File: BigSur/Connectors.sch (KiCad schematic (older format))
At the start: 15 parts, among them J1 XT30, J10 XT30, J11 XT30, J2 XT30, J3 XT30, J4 XT30, J5 XT30, J6 SMD CASTELLATION PKG, J7 XT30, J8 XT30, J9 XT30

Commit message: Added mounting holes, CAN connector,  indicator LEDs, started general purpose relays
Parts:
- removed J6: SMD CASTELLATION PKG, symbol Connector_Generic:Conn_02x21_Counter_Clockwise
- removed J?: XT30, symbol Connector_Generic:Conn_01x02
- added C28, C29: 0.1uF, symbol Device:C
- added D13: NUP2105L, Package_TO_SOT_SMD:SOT-23, symbol Device:D_TVS_x2_AAC
- added H1, H2, H3, H4: Hole, symbol Mechanical:MountingHole_Pad
- added J12: Conn_01x04, symbol Connector_Generic:Conn_01x04
- added J6: XT30, symbol Connector_Generic:Conn_01x02
- added SB1: Jumper_NC_Small, Jumper:SolderJumper-2_P1.3mm_Open_RoundedPad1.0x1.5mm, symbol Device:Jumper_NC_Small
- added U10: SMD42, GeneralMCU_Example:SMD42-FTP, symbol GeneralMCU-Example:SMD42
- TP1, TP2, TP3: footprint (none) -> TestPoint:TestPoint_Pad_D1.5mm
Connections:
- net labels added: GNDPWR, GP_RELAY_1_HIGH, GP_RELAY_1_LOW
- wire segments 92 -> 112
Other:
- note added: "CAN"
- note added: "GENERAL PURPOSE RELAYS"
- note added: "MOUNTING HOLES"
- note added: "NOT SURE IF WE NEED\nTEST POINTS ON THESE,\nCAN’T HURT THOUGH."
- note added: "POWER INPUT"
- note added: "POWER TEST POINTS"
- note added: "SOLENOIDS"
- note added: "STRIDEUINO"
- note removed: "CAN? (CANNOT?)"
- note removed: "CHASSIS GROUND… WHAT TO DO WITH YOU?"
- note removed: "NOT SURE IF WE EVEN NEED OR\nCARE ABOUT THESE, NOT A BIG\nDEAL TO ADD THEM THOUGH."
- note removed: "Power Input"
- note removed: "Power Test Points"
- note removed: "Solenoids"
- note removed: "Strideduino"
- note removed: "“Just do XT30 for everything” -Shane"
- moved on the sheet: J1, J10, J11, J2, J3, J4, J5, J7, J8, J9, TP1, TP2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

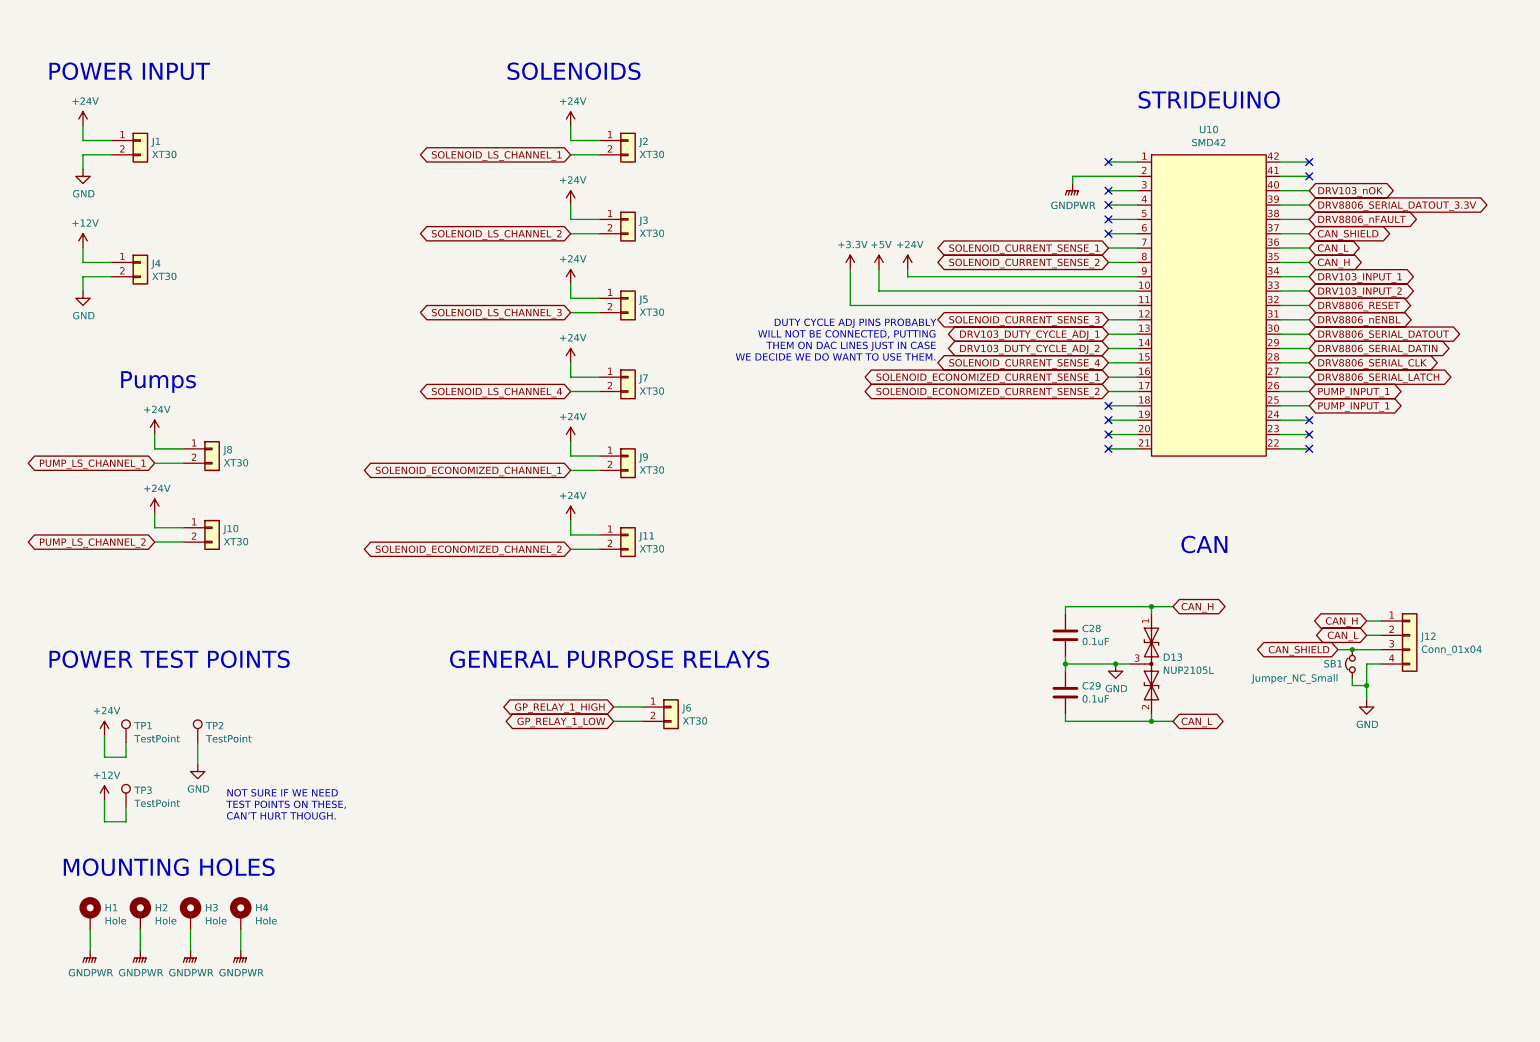
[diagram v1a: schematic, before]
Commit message: Updated test points
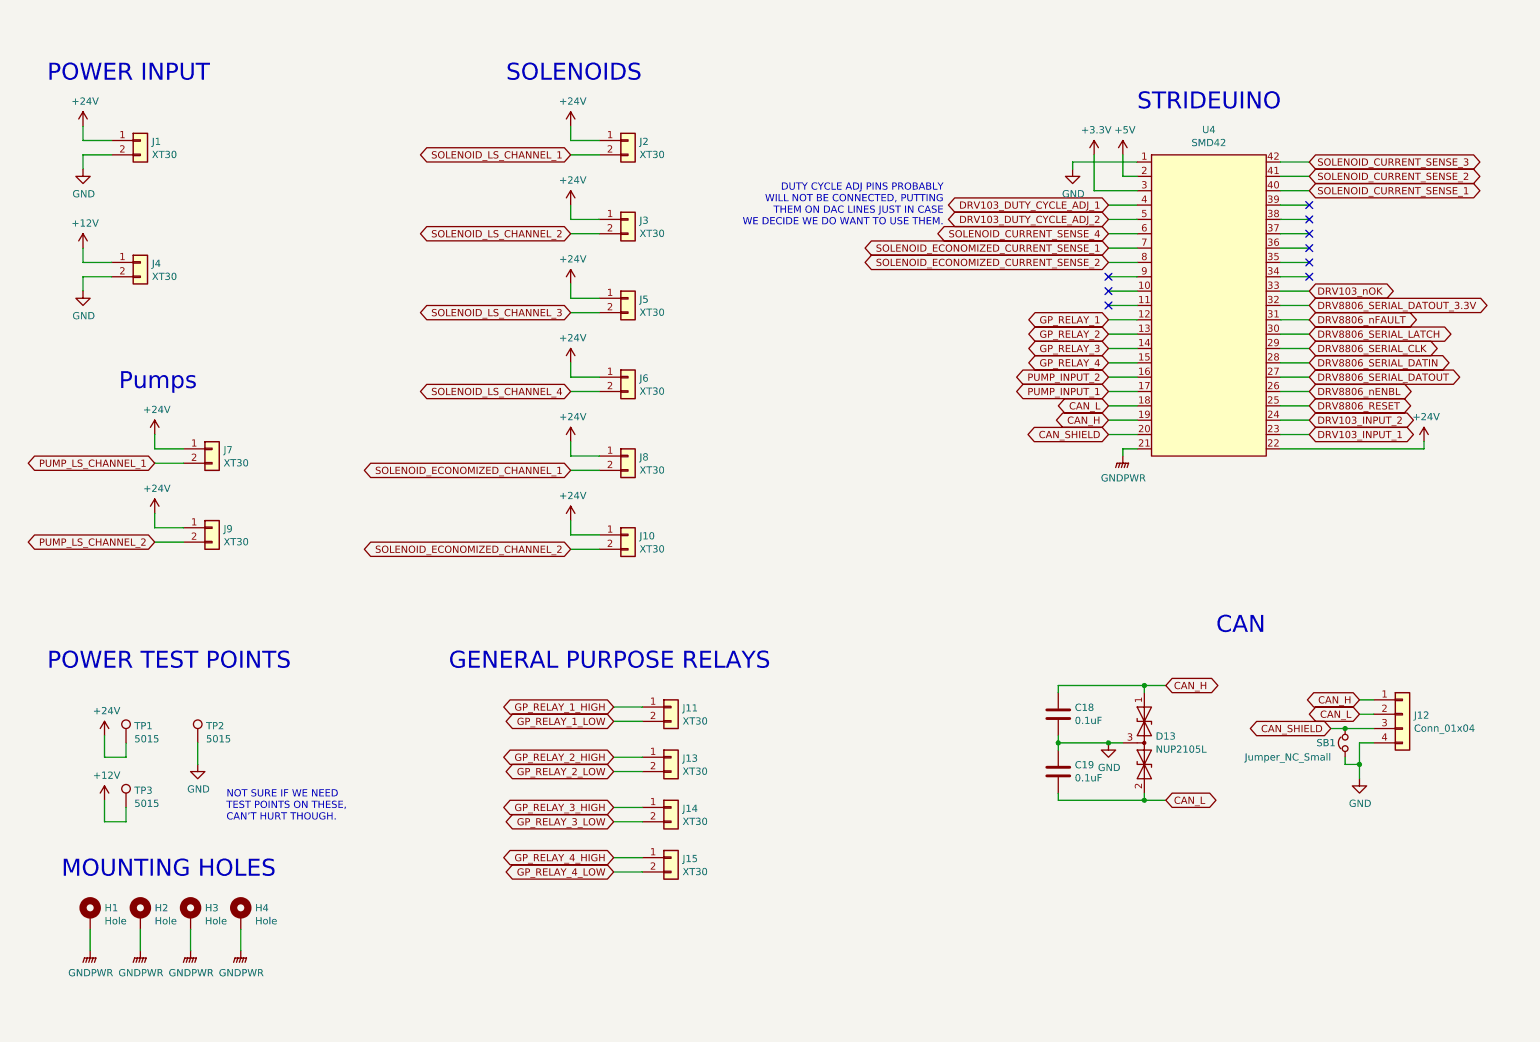
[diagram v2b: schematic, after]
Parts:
- removed C28, C29: 0.1uF, symbol Device:C
- added C18, C19: 0.1uF, Capacitor_SMD:C_0603_1608Metric_Pad1.05x0.95mm_HandSolder, symbol Device:C
- added J13, J14, J15: XT30, symbol Connector_Generic:Conn_01x02
- H1, H2, H3, H4: footprint (none) -> MountingHole:MountingHole_4.3mm_M4_Pad
- TP1, TP2, TP3: value TestPoint -> 5015; footprint TestPoint:TestPoint_Pad_D1.5mm -> BigSur:Keystone_TP_SMD_5015; Digikey (none) -> https://www.digikey.ca/product-detail/en/keystone-electroni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
- renumbered J11 to J10, J6 to J11, J7 to J6, J8 to J7, J9 to J8, J10 to J9, U10 to U4
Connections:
- net +24V: now also U4.22; no longer U4.9
- net +3V3: now also U4.3; no longer U4.11
- net +5V: now also U4.2; no longer U4.10
- net CAN_H: now also U4.19, C18.1; no longer U4.35
- net CAN_L: now also U4.18, C19.2; no longer U4.36
- net CAN_SHIELD: now also U4.20; no longer U4.37
- net DRV103_DUTY_CYCLE_ADJ_1: now also U4.4; no longer U4.13
- net DRV103_DUTY_CYCLE_ADJ_2: now also U4.5; no longer U4.14
- net DRV103_INPUT_1: now also U4.23; no longer U4.34
- net DRV103_INPUT_2: now also U4.24; no longer U4.33
- net DRV103_nOK: now also U4.33; no longer U4.40
- net DRV8806_RESET: now also U4.25; no longer U4.32
- net DRV8806_SERIAL_CLK: now also U4.29; no longer U4.28
- net DRV8806_SERIAL_DATIN: now also U4.28; no longer U4.29
- net DRV8806_SERIAL_DATOUT: now also U4.27; no longer U4.30
- net DRV8806_SERIAL_DATOUT_3.3V: now also U4.32; no longer U4.39
- net DRV8806_SERIAL_LATCH: now also U4.30; no longer U4.27
- net DRV8806_nENBL: now also U4.26; no longer U4.31
- net DRV8806_nFAULT: now also U4.31; no longer U4.38
- net GND: now also U4.1, C18.2, C19.1
- net GNDPWR: now also U4.21; no longer U4.2
- net PUMP_INPUT_1: now also U4.17; no longer U4.25, U4.26
- net SOLENOID_CURRENT_SENSE_1: now also U4.40; no longer U4.7
- net SOLENOID_CURRENT_SENSE_2: now also U4.41; no longer U4.8
- net SOLENOID_CURRENT_SENSE_3: now also U4.42; no longer U4.12
- net SOLENOID_CURRENT_SENSE_4: now also U4.6; no longer U4.15
- net SOLENOID_ECONOMIZED_CURRENT_SENSE_1: now also U4.7; no longer U4.16
- net SOLENOID_ECONOMIZED_CURRENT_SENSE_2: now also U4.8; no longer U4.17
- new net GP_RELAY_1: U4.12
- new net GP_RELAY_2: U4.13
- new net GP_RELAY_2_HIGH: J13.1 (Pin_1)
- new net GP_RELAY_2_LOW: J13.2 (Pin_2)
- new net GP_RELAY_3: U4.14
- new net GP_RELAY_3_HIGH: J14.1 (Pin_1)
- new net GP_RELAY_3_LOW: J14.2 (Pin_2)
- new net GP_RELAY_4: U4.15
- new net GP_RELAY_4_HIGH: J15.1 (Pin_1)
- new net GP_RELAY_4_LOW: J15.2 (Pin_2)
- new net PUMP_INPUT_2: U4.16
- no-connect marks 14 -> 9
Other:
- moved on the sheet: D13, J12, SB1

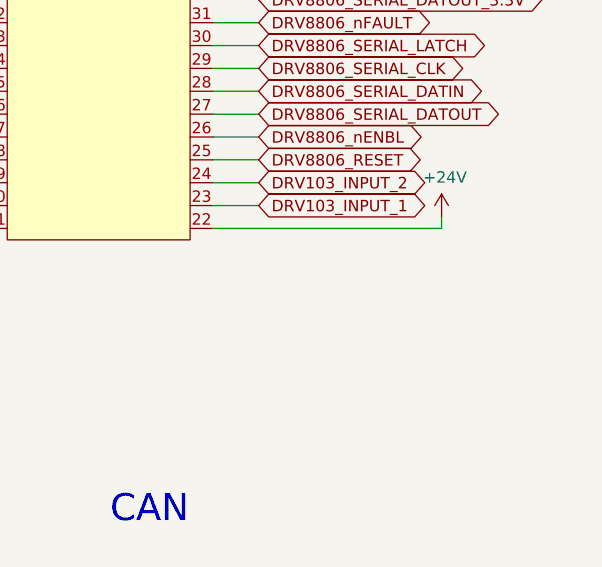
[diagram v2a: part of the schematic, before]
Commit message: Added braking detection, relay flyback, changed current sensors.
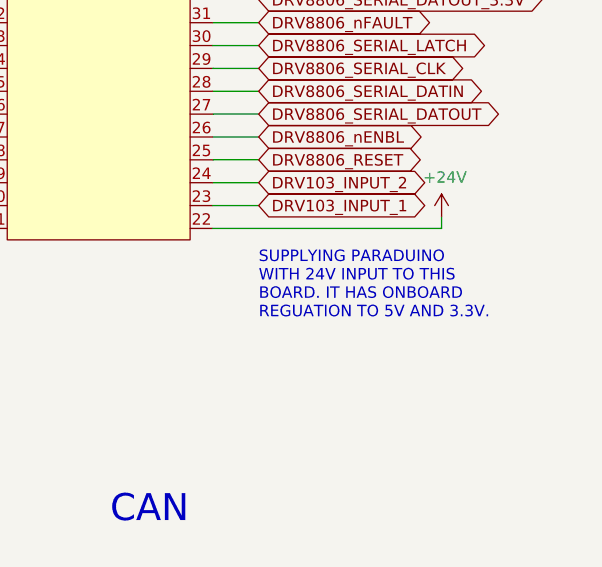
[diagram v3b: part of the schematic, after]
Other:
- note added: "SUPPLYING PARADUINO\nWITH 24V INPUT TO THIS\nBOARD. IT HAS ONBOARD\nREGUATION TO 5V AND 3.3V."
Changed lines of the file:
@@
 	1    0    0    -1
 $EndComp
+Text Notes 9650 4100 0    50   ~ 0
+SUPPLYING PARADUINO\nWITH 24V INPUT TO THIS\nBOARD. IT HAS ONBOARD\nREGUATION TO 5V AND 3.3V.
 $EndSCHEMATC

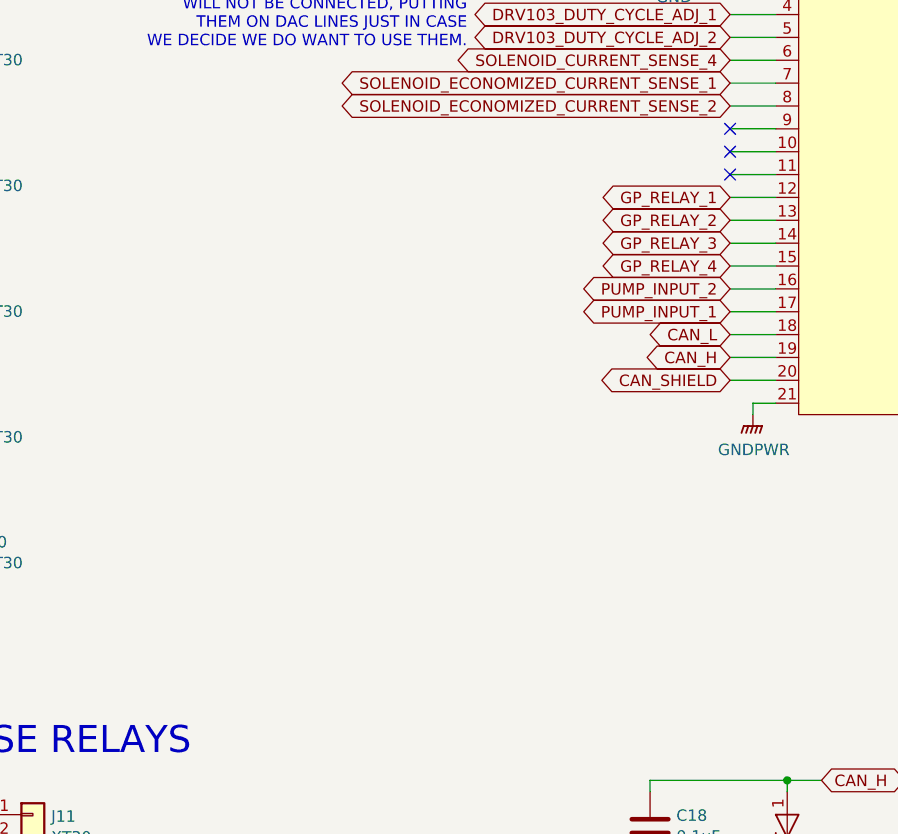
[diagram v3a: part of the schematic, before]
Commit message: Added inverter kill connectors.
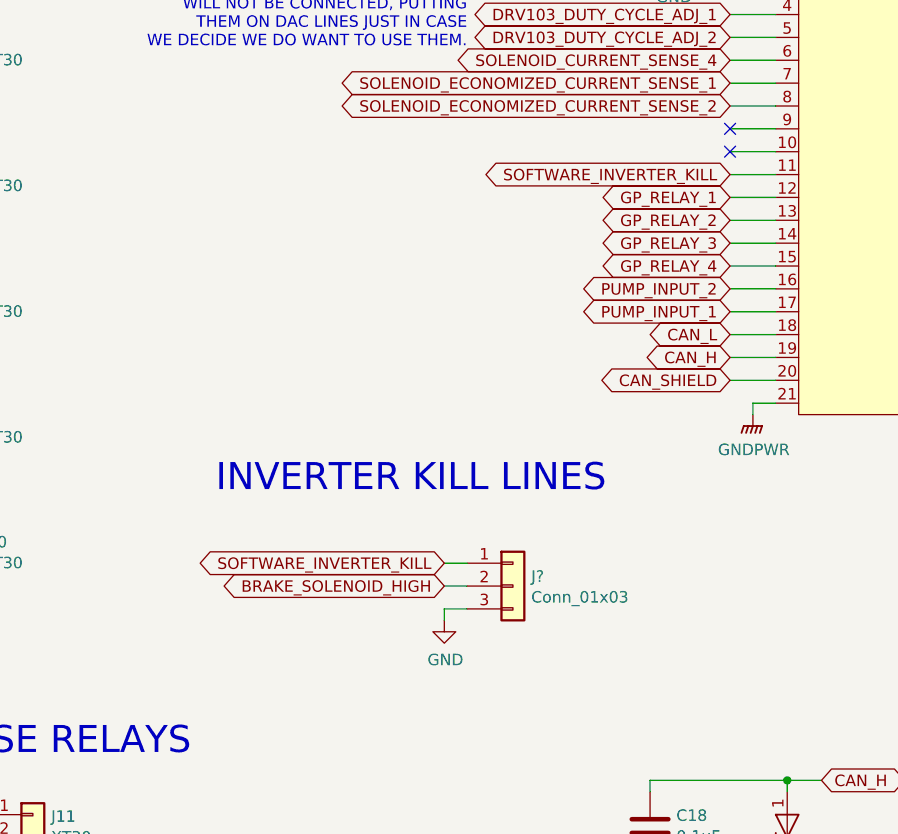
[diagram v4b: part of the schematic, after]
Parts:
- added J?: Conn_01x03, symbol Connector_Generic:Conn_01x03
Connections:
- net GND: now also J?.3 (Pin_3)
- net SOFTWARE_INVERTER_KILL: now reaches U4.11
- net SOFTWARE_INVERTER_KILL: now also J?.1 (Pin_1)
- new net BRAKE_SOLENOID_HIGH: J?.2 (Pin_2)
- no-connect marks 9 -> 8
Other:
- note added: "INVERTER KILL LINES"
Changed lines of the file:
@@
 Wire Wire Line
 	8250 2700 8450 2700
-NoConn ~ 8250 2700
 Wire Wire Line
 	8250 2800 8450 2800
@@
 Text Notes 9650 4100 0    50   ~ 0
 SUPPLYING PARADUINO\nWITH 24V INPUT TO THIS\nBOARD. IT HAS ONBOARD\nREGUATION TO 5V AND 3.3V.
+Text Notes 6000 4100 0    118  ~ 0
+INVERTER KILL LINES
+Text GLabel 8250 2700 0    50   BiDi ~ 0
+SOFTWARE_INVERTER_KILL
+$Comp
+L Connector_Generic:Conn_01x03 J?
+U 1 1 5DAB1B33
+P 7300 4500
+F 0 "J?" H 7380 4542 50  0000 L CNN
+F 1 "Conn_01x03" H 7380 4451 50  0000 L CNN
+F 2 "" H 7300 4500 50  0001 C CNN
+F 3 "~" H 7300 4500 50  0001 C CNN
+	1    7300 4500
+	1    0    0    -1
+$EndComp
+Text GLabel 7000 4400 0    50   BiDi ~ 0
+SOFTWARE_INVERTER_KILL
+Wire Wire Line
+	7000 4400 7100 4400
+Wire Wire Line
+	7100 4500 7000 4500
+Text GLabel 7000 4500 0    50   BiDi ~ 0
+BRAKE_SOLENOID_HIGH
+Wire Wire Line
+	7100 4600 7000 4600
+Wire Wire Line
+	7000 4600 7000 4650
+$Comp
+L power:GND #PWR?
+U 1 1 5DABF7D4
+P 7000 4650
+F 0 "#PWR?" H 7000 4400 50  0001 C CNN
+F 1 "GND" H 7005 4477 50  0000 C CNN
+F 2 "" H 7000 4650 50  0001 C CNN
+F 3 "" H 7000 4650 50  0001 C CNN
+	1    7000 4650
+	1    0    0    -1
+$EndComp
 $EndSCHEMATC

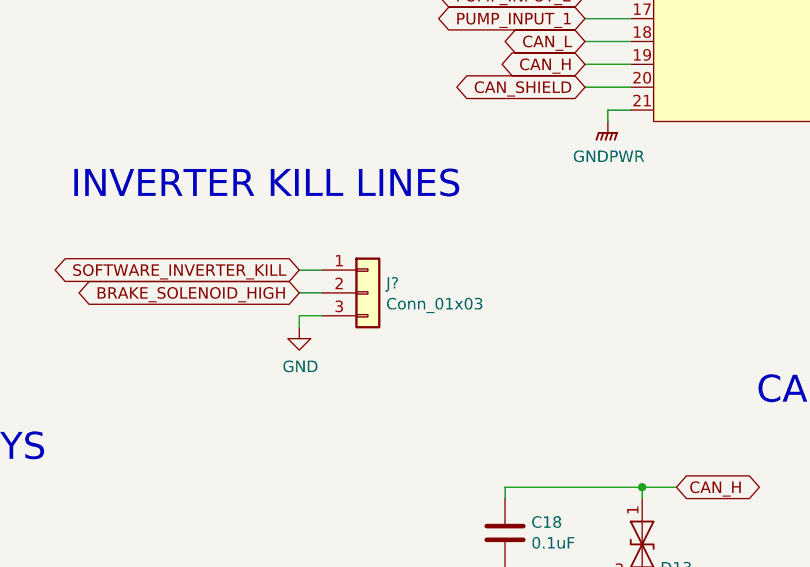
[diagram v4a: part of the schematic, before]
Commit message: Fixed current sense, added GP relay LEDs
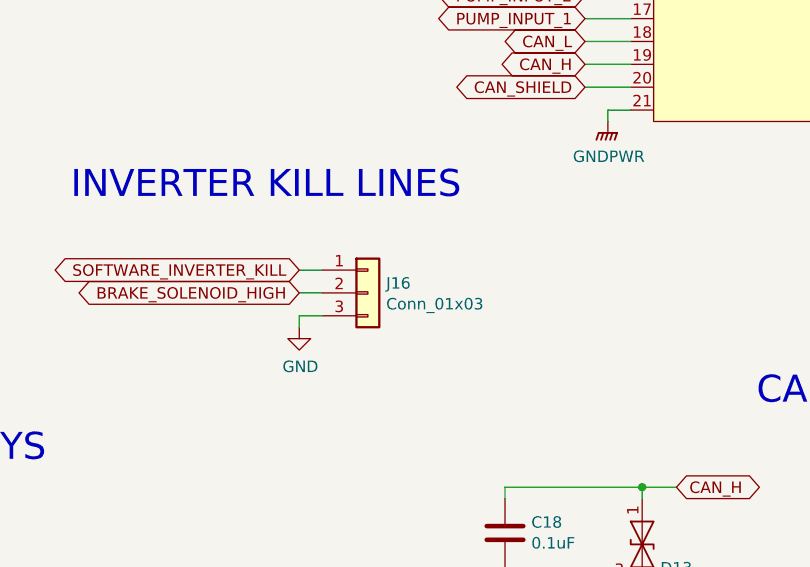
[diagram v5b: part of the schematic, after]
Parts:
- gave numbers to parts that had none: 1
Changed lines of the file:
@@
 SOFTWARE_INVERTER_KILL
 $Comp
-L Connector_Generic:Conn_01x03 J?
+L Connector_Generic:Conn_01x03 J16
 U 1 1 5DAB1B33
 P 7300 4500
-F 0 "J?" H 7380 4542 50  0000 L CNN
+F 0 "J16" H 7380 4542 50  0000 L CNN
 F 1 "Conn_01x03" H 7380 4451 50  0000 L CNN
 F 2 "" H 7300 4500 50  0001 C CNN
@@
 	7000 4600 7000 4650
 $Comp
-L power:GND #PWR?
+L power:GND #PWR0118
 U 1 1 5DABF7D4
 P 7000 4650
-F 0 "#PWR?" H 7000 4400 50  0001 C CNN
+F 0 "#PWR0118" H 7000 4400 50  0001 C CNN
 F 1 "GND" H 7005 4477 50  0000 C CNN
 F 2 "" H 7000 4650 50  0001 C CNN
